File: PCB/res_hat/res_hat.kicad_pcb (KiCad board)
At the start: 2 copper layers, 85 x 56 mm, 55 parts, among them IC1 MCP4725A0T-E_CH, IC2 MCP4725A0T-E_CH, IC3 UCC27324D, J1 Conn_02x20_Odd_Even, J10 Conn_01x02, J11 Jack-DC, J2 Conn_02x04_Odd_Even, J3 Conn_01x03, J4 Conn_01x06, J5 Conn_Coaxial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

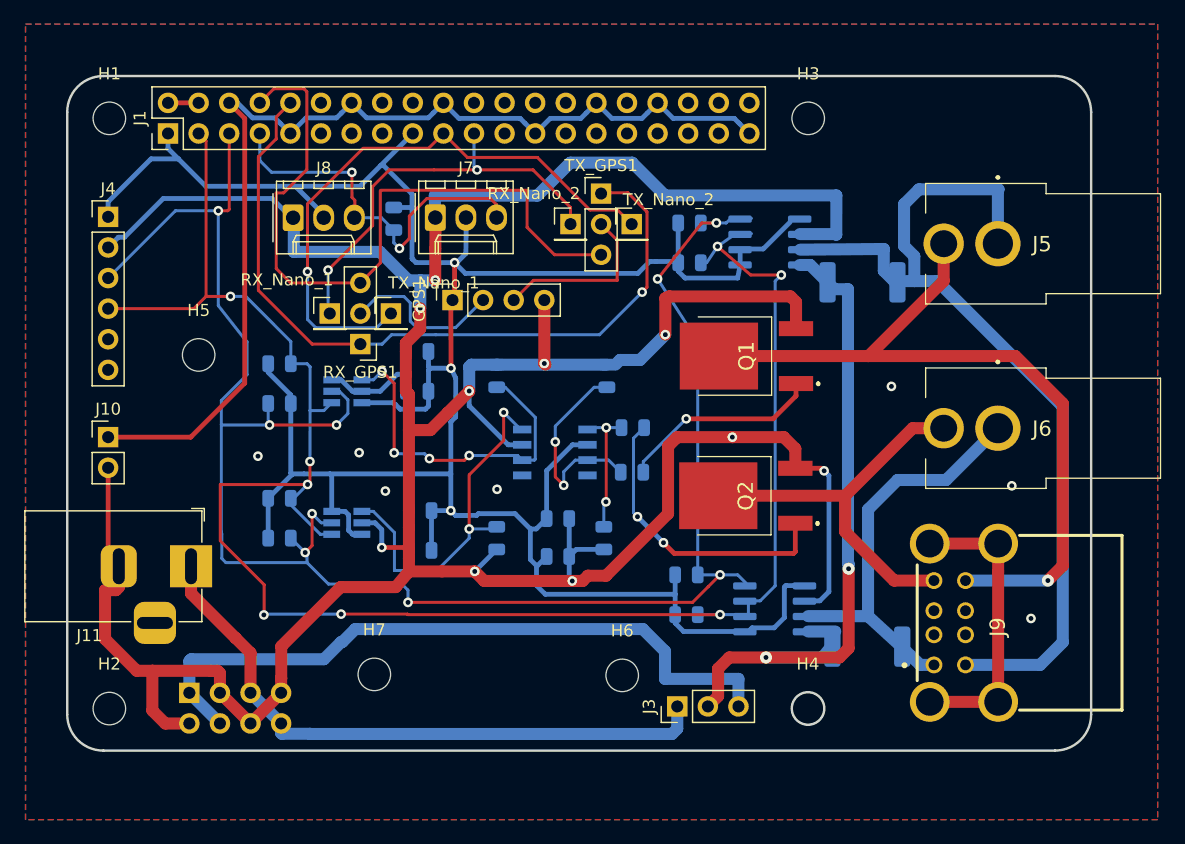
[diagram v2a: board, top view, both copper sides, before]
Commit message: change DC for XT30, change controle res for pwm
add ds1050Z-025+ change for xt30 connector for in alim
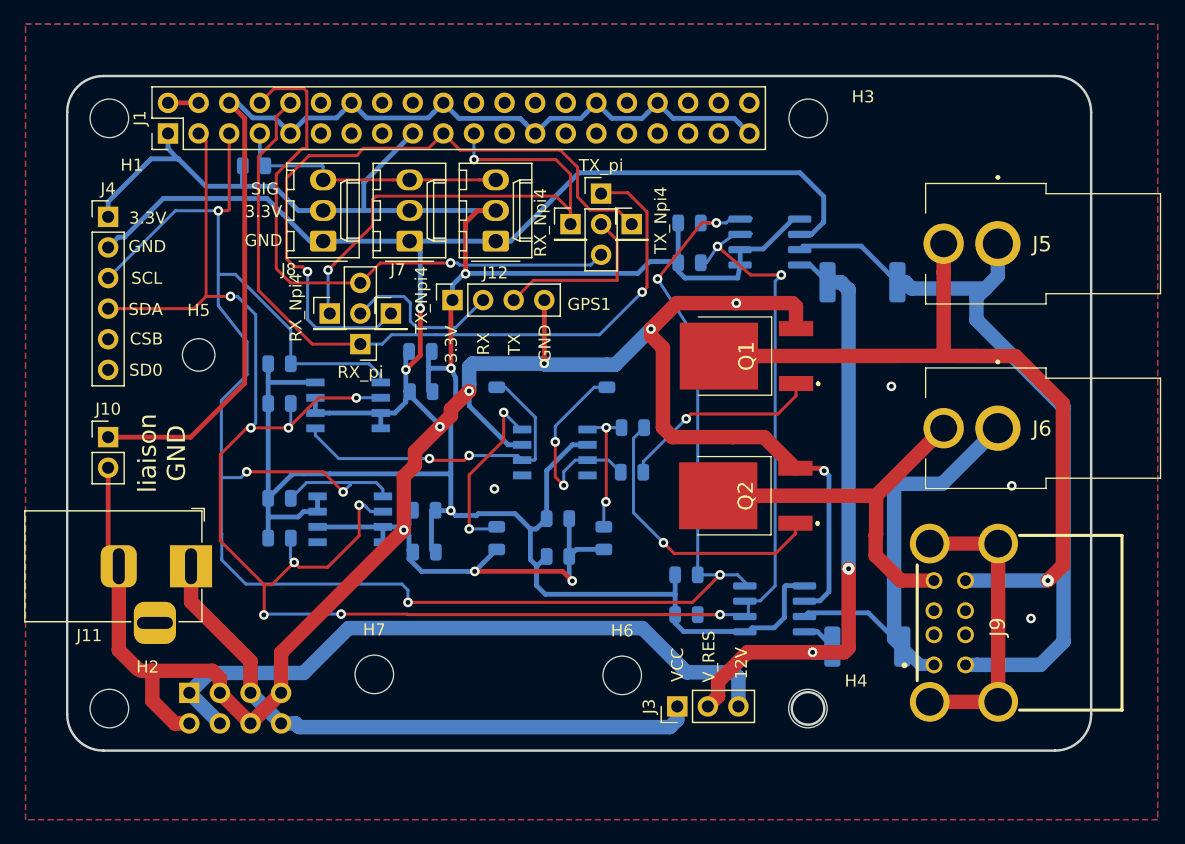
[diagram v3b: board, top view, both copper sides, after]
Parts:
- added J12: Conn_01x03, Connector_Molex:Molex_KK-254_AE-6410-03A_1x03_P2.54mm_Vertical, F.Cu at (97.5, 112.0)
- IC1, IC2: value MCP4725A0T-E_CH -> DS1050Z-025+; footprint mcp4725:SOT95P270X145-6N -> DS1050Z:SOIC127P600X175-8N
- moved R15 12.4 mm to (77.4, 105.7), turned to 180 degrees
- moved J8 3.16 mm to (83.1, 112.0), turned to 90 degrees
- moved J7 2.89 mm to (90.3, 112.0), turned to 90 degrees
- moved IC1 1.18 mm to (85.2, 125.6)
- moved IC2 0.41 mm to (85.4, 135.1)
- moved C3 0.39 mm to (91.5, 137.8)
- moved C2 0.35 mm to (91.3, 124.5)
- moved C4 0.33 mm to (91.5, 134.3)
- moved C1 0.27 mm to (91.2, 121.2)
- turned R1 to 0 degrees
- renumbered RX_Nano_2 to RX_Npi4, RX_Nano_1 to RX_Npi4, RX_GPS1 to RX_pi, TX_Nano_2 to TX_Npi4, TX_Nano_1 to TX_Npi4, TX_GPS1 to TX_pi
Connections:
- IC1 pad 1: Net-(IC1-Pad1) -> /SCL
- IC1 pad 2: GND -> /SDA
- IC1 pad 3: +3V3 -> GND
- IC1 pad 4: /SDA -> GND
- IC1 pad 5: /SCL -> Net-(IC1-Pad5)
- IC2 pad 1: Net-(IC2-Pad1) -> /SCL
- IC2 pad 2: GND -> /SDA
- IC2 pad 3: +3V3 -> GND
- IC2 pad 4: /SDA -> GND
- IC2 pad 5: /SCL -> Net-(IC2-Pad5)
- IC2 pad 6: +3V3 -> GND
- IC3 pad 1: Net-(IC3-Pad1) -> (no net)
- IC3 pad 2: Net-(IC1-Pad1) -> Net-(IC1-Pad5)
- IC3 pad 4: Net-(IC2-Pad1) -> Net-(IC2-Pad5)
- IC3 pad 8: Net-(IC3-Pad8) -> (no net)
- J1 pad 11: Net-(J1-Pad11) -> (no net)
- J1 pad 12: Net-(J1-Pad12) -> (no net)
- J1 pad 13: Net-(J1-Pad13) -> (no net)
- J1 pad 15: Net-(J1-Pad15) -> (no net)
- J1 pad 16: Net-(J1-Pad16) -> (no net)
- J1 pad 18: Net-(J1-Pad18) -> (no net)
- J1 pad 22: Net-(J1-Pad22) -> (no net)
- J1 pad 23: Net-(J1-Pad23) -> (no net)
- J1 pad 24: Net-(J1-Pad24) -> (no net)
- J1 pad 26: Net-(J1-Pad26) -> (no net)
- J1 pad 27: Net-(J1-Pad27) -> (no net)
- J1 pad 28: Net-(J1-Pad28) -> (no net)
- J1 pad 29: Net-(J1-Pad29) -> (no net)
- J1 pad 31: Net-(J1-Pad31) -> (no net)
- J1 pad 32: Net-(J1-Pad32) -> (no net)
- J1 pad 33: Net-(J1-Pad33) -> (no net)
- J1 pad 35: Net-(J1-Pad35) -> (no net)
- J1 pad 36: Net-(J1-Pad36) -> (no net)
- J1 pad 37: Net-(J1-Pad37) -> (no net)
- J1 pad 38: Net-(J1-Pad38) -> (no net)
- J1 pad 40: Net-(J1-Pad40) -> (no net)
- J4 pad 5: /CSB -> (no net)
- J4 pad 6: /SDO -> (no net)
- J9 pad 2: Net-(J9-Pad2) -> (no net)
- J9 pad 3: Net-(J9-Pad3) -> (no net)
- J9 pad 6: Net-(J9-Pad6) -> (no net)
- J9 pad 7: Net-(J9-Pad7) -> (no net)
- R1 pad 2: /SCL -> /SDA
- R2 pad 2: /SCL -> /SDA
- R3 pad 2: /SDA -> /SCL
- R4 pad 2: /SDA -> /SCL
- R5 pad 1: Net-(IC2-Pad1) -> Net-(IC2-Pad5)
- R6 pad 2: Net-(IC1-Pad1) -> Net-(IC1-Pad5)
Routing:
- net Net-(IC2-Pad1): track 30.0 -> 0.00 mm, vias 2 -> 0
- net Net-(IC1-Pad1): track 29.2 -> 0.00 mm, vias 4 -> 0
- net Net-(IC1-Pad5): track 0.00 -> 27.8 mm, vias 0 -> 2
- net /SCL: track 158.9 -> 176.5 mm, vias 9 -> 7
- net Net-(IC2-Pad5): track 0.00 -> 15.3 mm, vias 0 -> 2
- net Net-(J5-Pad1): track 76.3 -> 62.9 mm
- net /SDA: track 156.5 -> 169.3 mm, vias 8 -> 11
- net /UART_RX_NanopiM4: track 34.9 -> 45.4 mm
- net /UART_TX: track 58.8 -> 49.0 mm, vias 0 -> 1
- net /1-Wire: track 33.3 -> 25.4 mm, vias 2 -> 0
- net /UART_TX_NanopiM4: track 49.7 -> 55.3 mm
- net Net-(J5-Pad2): track 64.1 -> 68.5 mm
- net VD: track 57.9 -> 53.8 mm
- net GND: track 300.4 -> 297.5 mm, vias 17 -> 15
- net +12V: track 58.3 -> 55.5 mm
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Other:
- board text added: "12V"
- board text added: "3.3V"
- board text added: "CSB"
- board text added: "GND"
- board text added: "RX"
- board text added: "SCL"
- board text added: "SD0"
- board text added: "SDA"
- board text added: "SIG"
- board text added: "TX"
- board text added: "VCC"
- board text added: "V_RES"
- board text added: "liaison GND"

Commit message: update alim and relais pcb 2-> 4 couches
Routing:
- net Net-(IC2-Pad5): track 15.3 -> 30.7 mm, vias 2 -> 3
- net GND: vias 15 -> 16

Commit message: ajust all board
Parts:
- Q1, Q2: moved to B.Cu
- moved R11 0.15 mm to (127.9, 115.3)
- turned Q1 to 270 degrees
- turned Q2 to 270 degrees
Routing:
- net GND: track 297.5 -> 343.5 mm, vias 16 -> 23
- net /SDA: track 169.3 -> 183.3 mm
- net Net-(Q1-Pad1): track 16.8 -> 28.1 mm, vias 1 -> 2
- net Net-(J5-Pad1): track 62.9 -> 74.0 mm
- net VCC: track 50.5 -> 58.6 mm
- net VD: track 53.8 -> 61.1 mm, vias 2 -> 8
- net Net-(J6-Pad2): track 31.7 -> 37.6 mm
- net Net-(J6-Pad1): track 35.9 -> 39.1 mm
- net Net-(J5-Pad2): track 68.5 -> 65.4 mm, vias 1 -> 8
- net Net-(Q2-Pad1): track 24.0 -> 21.4 mm, vias 1 -> 2
- net +12V: track 55.5 -> 56.3 mm
- net /SCL: track 176.5 -> 177.1 mm

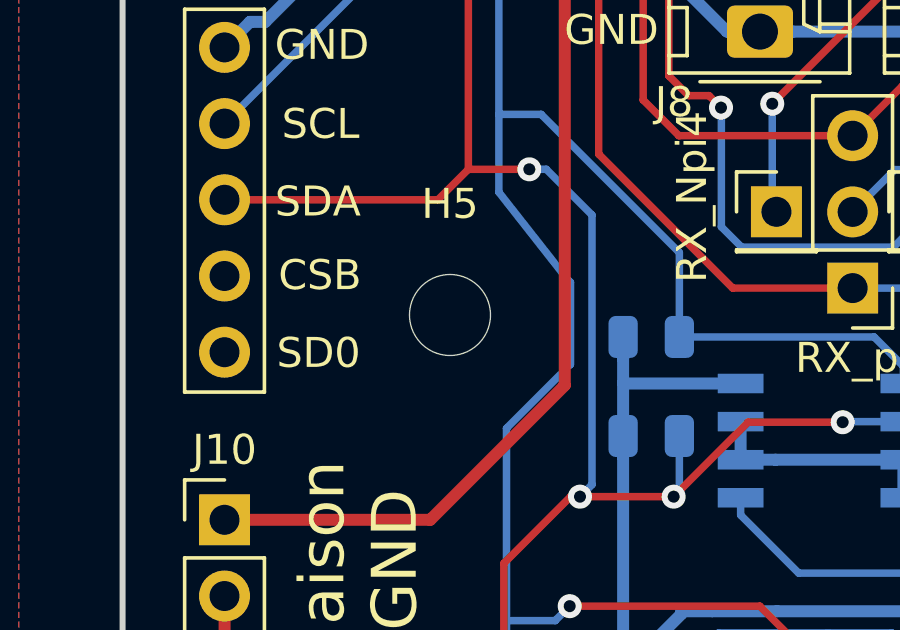
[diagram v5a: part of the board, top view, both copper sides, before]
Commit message: ajust terminal position in relay board
change hole diameter in res_board
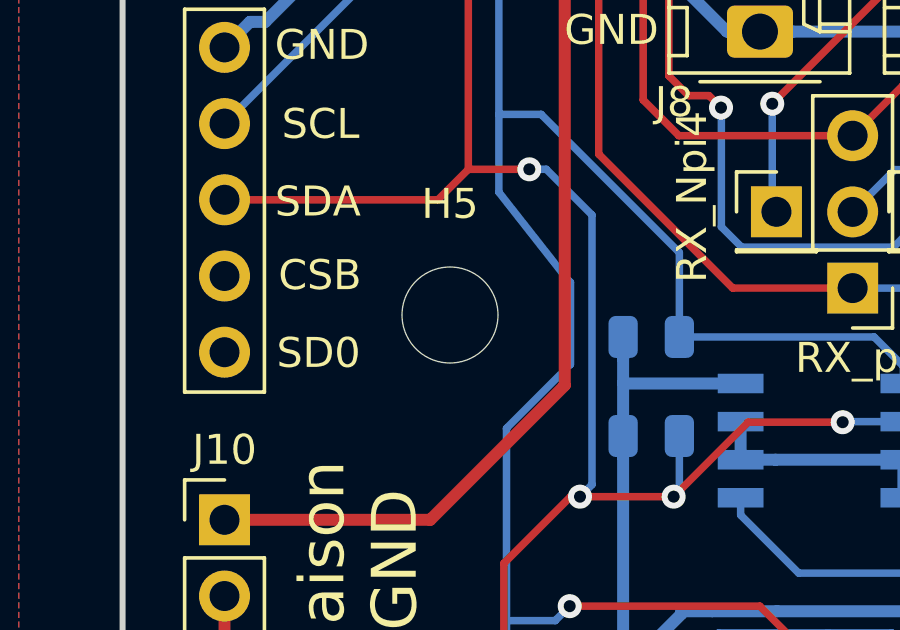
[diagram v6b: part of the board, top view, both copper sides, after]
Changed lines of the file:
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@@
       (effects (font (size 1 1) (thickness 0.15)))
     )
-    (pad 1 np_thru_hole circle (at 0 0) (size 2.7 2.7) (drill 2.7) (layers *.Cu *.Mask))
+    (pad "" np_thru_hole circle (at 0 0) (size 3.2 3.2) (drill 3.2) (layers *.Cu *.Mask))
   )
   (module Connector_PinHeader_2.54mm:PinHeader_1x02_P2.54mm_Vertical (layer F.Cu)
